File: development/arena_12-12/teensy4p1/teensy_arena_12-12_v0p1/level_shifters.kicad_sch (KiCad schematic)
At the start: 15 parts, among them U1 TXB0108PW, U2 TXB0108PW, U3 TXB0108PW, U4 TXB0108PW, U5 TXB0108PW

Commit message: Worked on 12-12 teensy4p1 arena without vreg.
Modified SPI connections from teensy to panel columns so that all
signals go from a single source to a single destinatin. Also, added
source termination resistors and schmitt trigger buffers to all SPI
signals.
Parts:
- removed U4, U5: TXB0108PW, Package_SO:TSSOP-20_4.4x6.5mm_P0.65mm, symbol TXB0108:TXB0108PW
- added C13, C14, C15, C16, C17, C18, C19, C20, C21, C22, C23, C24, C25, C26, C27, C28, C29, C30, C31, C32, C33, C34, C35, C36, C37, C38, C39, C40, C41, C42, C43, C44, C45, C46, C47, C48, C49, C50, C51, C52, C53, C54, C55, C56, C57, C58, C59, C60, C61, C62, C63, C64: 0.1uF, Capacitor_SMD:C_0603_1608Metric, symbol Device:C
- added R100, R101, R102, R103, R104, R105, R106, R107, R108, R109, R110, R111, R112, R113, R114, R115, R116, R117, R118, R119, R120, R121, R122, R123, R124, R125, R126, R39, R40, R41, R42, R43, R44, R45, R46, R47, R48, R49, R50, R51, R52, R53, R54, R55, R56, R57, R58, R59, R60, R61, R62, R63, R64, R65, R66, R67, R68, R69, R70, R71, R72, R73, R74, R75, R76, R77, R78, R79, R80, R81, R82, R83, R84, R85, R86, R87, R88, R89, R90, R91, R92, R93, R94, R95, R96, R97, R98, R99: 68, symbol Device:R
- added U10, U11, U12, U13, U14, U15, U7, U8, U9: TXB0108PW, Package_SO:TSSOP-20_4.4x6.5mm_P0.65mm, symbol TXB0108:TXB0108PW
- added U16, U17, U18, U19, U20, U21, U22, U23, U24, U25, U26, U27, U28, U29, U30, U31, U32, U33, U34, U35, U36, U37, U38, U39, U40, U41, U42, U43, U44, U45, U46, U47, U48, U49, U50, U51, U52, U53: 74LVC1G17, symbol 74xGxx:74LVC1G17
- renumbered C8 to C10, C9 to C11, C10 to C12, C1 to C3, C2 to C4, C3 to C5, C4 to C6, C5 to C7, C6 to C8, C7 to C9, U1 to U4, U2 to U5, U3 to U6
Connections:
- net +3.3V: now also C13.1, C15.1, C17.1, C19.1, C21.1, C23.1, C25.1, C27.1, C28.1, C29.1, C30.1, C31.1, C32.1, C33.1, C34.1, C35.1, C36.1, C37.1, C38.1, C39.1, C40.1, C41.1, C42.1, C43.1, C44.1, C45.1, C46.1, C47.1, C48.1, C49.1, C50.1, C51.1, C52.1, C53.1, C54.1, C55.1, C56.1, C57.1, C58.1, C59.1, C60.1, C61.1, C62.1, U10.10 (OE), U10.2 (VCCA), U11.10 (OE), U11.2 (VCCA), U12.10 (OE), U12.2 (VCCA), U13.10 (OE), U13.2 (VCCA), U14.10 (OE), U14.2 (VCCA), U15.10 (OE), U15.2 (VCCA), U16.5 (VCC), U17.5 (VCC), U18.5 (VCC), U19.5 (VCC), U20.5 (VCC), U21.5 (VCC), U22.5 (VCC), U23.5 (VCC), U24.5 (VCC), U25.5 (VCC), U26.5 (VCC), U27.5 (VCC), U28.5 (VCC), U29.5 (VCC), U30.5 (VCC), U31.5 (VCC), U32.5 (VCC), U33.5 (VCC), U34.5 (VCC), U35.5 (VCC), U36.5 (VCC), U37.5 (VCC), U38.5 (VCC), U39.5 (VCC), U40.5 (VCC), U41.5 (VCC), U42.5 (VCC), U43.5 (VCC), U44.5 (VCC), U45.5 (VCC), U46.5 (VCC), U47.5 (VCC), U48.5 (VCC), U49.5 (VCC), U50.5 (VCC), U51.5 (VCC), U7.10 (OE), U7.2 (VCCA), U8.10 (OE), U8.2 (VCCA), U9.10 (OE), U9.2 (VCCA)
- net +5V: now also C14.1, C16.1, C18.1, C20.1, C22.1, C24.1, C26.1, C63.1, C64.1, U10.19 (VCCB), U11.19 (VCCB), U12.19 (VCCB), U13.19 (VCCB), U14.19 (VCCB), U15.19 (VCCB), U52.5 (VCC), U53.5 (VCC), U7.19 (VCCB), U8.19 (VCCB), U9.19 (VCCB)
- net GND: now also C13.2, C14.2, C15.2, C16.2, C17.2, C18.2, C19.2, C20.2, C21.2, C22.2, C23.2, C24.2, C25.2, C26.2, C27.2, C28.2, C29.2, C30.2, C31.2, C32.2, C33.2, C34.2, C35.2, C36.2, C37.2, C38.2, C39.2, C40.2, C41.2, C42.2, C43.2, C44.2, C45.2, C46.2, C47.2, C48.2, C49.2, C50.2, C51.2, C52.2, C53.2, C54.2, C55.2, C56.2, C57.2, C58.2, C59.2, C60.2, C61.2, C62.2, C63.2, C64.2, U10.11 (GND), U11.11 (GND), U12.11 (GND), U13.11 (GND), U14.11 (GND), U15.11 (GND), U16.3 (GND), U17.3 (GND), U18.3 (GND), U19.3 (GND), U20.3 (GND), U21.3 (GND), U22.3 (GND), U23.3 (GND), U24.3 (GND), U25.3 (GND), U26.3 (GND), U27.3 (GND), U28.3 (GND), U29.3 (GND), U30.3 (GND), U31.3 (GND), U32.3 (GND), U33.3 (GND), U34.3 (GND), U35.3 (GND), U36.3 (GND), U37.3 (GND), U38.3 (GND), U39.3 (GND), U40.3 (GND), U41.3 (GND), U42.3 (GND), U43.3 (GND), U44.3 (GND), U45.3 (GND), U46.3 (GND), U47.3 (GND), U48.3 (GND), U49.3 (GND), U50.3 (GND), U51.3 (GND), U52.3 (GND), U53.3 (GND), U7.11 (GND), U8.11 (GND), U9.11 (GND)
- net PAN3V.CS_00: now also U20.2; no longer U5.1 (A1)
- net PAN3V.CS_01: now also U21.2; no longer U5.3 (A2)
- net PAN3V.CS_02: now also U22.2; no longer U5.4 (A3)
- net PAN3V.CS_03: now also U23.2; no longer U5.5 (A4)
- net PAN3V.CS_04: now also U24.2; no longer U5.6 (A5)
- net PAN3V.CS_05: now also U25.2; no longer U5.7 (A6)
- net PAN3V.CS_06: now also U26.2; no longer U5.8 (A7)
- net PAN3V.CS_07: now also U27.2; no longer U5.9 (A8)
- net PAN3V.CS_08: now also U28.2; no longer U6.1 (A1)
- net PAN3V.CS_09: now also U29.2; no longer U6.3 (A2)
- net PAN3V.CS_10: now also U30.2; no longer U6.4 (A3)
- net PAN3V.CS_11: now also U31.2; no longer U6.5 (A4)
- net PAN3V.CS_12: now also U32.2; no longer U6.6 (A5)
- net PAN3V.CS_13: now also U33.2; no longer U6.7 (A6)
- net PAN3V.CS_14: now also U34.2; no longer U6.8 (A7)
- net PAN3V.CS_15: now also U35.2; no longer U6.9 (A8)
- net PAN3V.CS_16: now also U36.2
- net PAN3V.CS_17: now also U37.2
- net PAN3V.CS_18: now also U38.2
- net PAN3V.CS_19: now also U39.2
- net PAN3V.CS_20: now also U40.2
- net PAN3V.CS_21: now also U41.2
- net PAN3V.CS_22: now also U42.2
- net PAN3V.CS_23: now also U43.2
- net PAN3V.CS_24: now also U44.2
- net PAN3V.CS_25: now also U45.2
- net PAN3V.CS_26: now also U46.2
- net PAN3V.CS_27: now also U47.2
- net PAN3V.CS_28: now also U48.2
- net PAN3V.CS_29: now also U49.2
- net PAN3V.EXT_INT: now also U51.2
- net PAN3V.MISO_0: now also R125.1; no longer U4.5 (A4)
- net PAN3V.MISO_1: now also R126.1; no longer U4.9 (A8)
- net PAN3V.MOSI_0: now also U17.2; no longer U4.4 (A3)
- net PAN3V.MOSI_1: now also U19.2; no longer U4.8 (A7)
- net PAN3V.RESET: now also U50.2; no longer U4.1 (A1)
- net PAN3V.SCK_0: now also U16.2; no longer U4.3 (A2)
- net PAN3V.SCK_1: now also U18.2; no longer U4.7 (A6)
- net PAN5V.EXT_INT: now also R124.1
- net PAN5V.MISO_0: now also U52.2; no longer U4.16 (B4)
- net PAN5V.MISO_1: now also U53.2; no longer U4.12 (B8)
- net PAN5V.RESET: now also R123.1; no longer U4.20 (B1)
- net PAN5V.CS_00: no longer names the net of U5.20 (B1)
- net PAN5V.CS_00: now also R45.2
- net PAN5V.CS_01: no longer names the net of U5.18 (B2)
- net PAN5V.CS_01: now also R46.2
- net PAN5V.CS_02: no longer names the net of U5.17 (B3)
- net PAN5V.CS_03: no longer names the net of U5.16 (B4)
- net PAN5V.CS_03: now also R47.2
- net PAN5V.CS_04: no longer names the net of U5.15 (B5)
- net PAN5V.CS_05: no longer names the net of U5.14 (B6)
- net PAN5V.CS_05: now also R48.2
- net PAN5V.CS_06: no longer names the net of U5.13 (B7)
- net PAN5V.CS_06: now also R49.2
- net PAN5V.CS_07: no longer names the net of U5.12 (B8)
- net PAN5V.CS_07: now also R50.2
- net PAN5V.CS_08: no longer names the net of U6.20 (B1)
- net PAN5V.CS_08: now also R51.2
- net PAN5V.CS_09: no longer names the net of U6.18 (B2)
- net PAN5V.CS_09: now also R52.2
- net PAN5V.CS_10: no longer names the net of U6.17 (B3)
- net PAN5V.CS_11: no longer names the net of U6.16 (B4)
- net PAN5V.CS_11: now also R53.2
- net PAN5V.CS_12: no longer names the net of U6.15 (B5)
- net PAN5V.CS_13: no longer names the net of U6.14 (B6)
- net PAN5V.CS_13: now also R54.2
- net PAN5V.CS_14: no longer names the net of U6.13 (B7)
- net PAN5V.CS_14: now also R55.2
- net PAN5V.CS_15: no longer names the net of U6.12 (B8)
- net PAN5V.CS_15: now also R56.2
- net PAN5V.MOSI_0: no longer names the net of U4.17 (B3)
- net PAN5V.MOSI_1: no longer names the net of U4.13 (B7)
- net PAN5V.MOSI_1: now also R43.2
- net PAN5V.SCK_0: no longer names the net of U4.18 (B2)
- net PAN5V.SCK_0: now also R40.2
- net PAN5V.SCK_1: no longer names the net of U4.14 (B6)
- net PAN5V.SCK_1: now also R42.2
- new net: U11.1 (A1), U11.3 (A2), U32.4
- new net: R94.2, U11.12 (B8)
- new net: R93.2, U11.13 (B7)
- new net: R92.2, U11.14 (B6)
- new net: R91.2, U11.15 (B5)
- new net: R90.2, U11.16 (B4)
- new net: R89.2, U11.17 (B3)
- new net: R88.2, U11.18 (B2)
- new net: R87.2, U11.20 (B1)
- new net: U11.4 (A3), U11.5 (A4), U33.4
- new net: U11.6 (A5), U11.7 (A6), U34.4
- new net: U11.8 (A7), U11.9 (A8), U35.4
- new net: R57.2, U7.20 (B1)
- new net: R122.2, U15.16 (B4)
- new net: R102.2, U12.12 (B8)
- new net: R86.2, U10.12 (B8)
- new net: R108.2, U13.14 (B6)
- new net: U21.4, U8.4 (A3), U8.5 (A4)
- new net: U13.1 (A1), U13.3 (A2), U40.4
- new net: R107.2, U13.15 (B5)
- new net: U15.1 (A1), U15.3 (A2), U48.4
- new net: R64.2, U8.17 (B3)
- new net: R79.2, U10.20 (B1)
- new net: U14.6 (A5), U14.7 (A6), U46.4
- new net: R73.2, U9.17 (B3)
- new net: U15.12 (B8), U53.4
- new net: U15.13 (B7), U52.4
- new net: R124.2, U15.14 (B6)
- new net: R123.2, U15.15 (B5)
- new net: R121.2, U15.17 (B3)
- new net: R120.2, U15.18 (B2)
- new net: R119.2, U15.20 (B1)
- new net: U15.4 (A3), U15.5 (A4), U49.4
- new net: U15.6 (A5), U50.4
- new net: U15.7 (A6), U51.4
- new net: R125.2, U15.8 (A7)
- new net: R126.2, U15.9 (A8)
- new net: R83.2, U10.15 (B5)
- new net: R77.2, U9.13 (B7)
- new net: R116.2, U14.14 (B6)
- new net: U27.4, U9.8 (A7), U9.9 (A8)
- new net: R68.2, U8.13 (B7)
- new net: R78.2, U9.12 (B8)
- new net: U13.6 (A5), U13.7 (A6), U42.4
- new net: R59.2, U7.16 (B4)
- new net: U14.1 (A1), U14.3 (A2), U44.4
- new net: R118.2, U14.12 (B8)
- new net: R117.2, U14.13 (B7)
- new net: R115.2, U14.15 (B5)
- new net: R114.2, U14.16 (B4)
- new net: R113.2, U14.17 (B3)
- new net: R112.2, U14.18 (B2)
- new net: R111.2, U14.20 (B1)
- new net: U14.4 (A3), U14.5 (A4), U45.4
- new net: U14.8 (A7), U14.9 (A8), U47.4
- new net: R97.2, U12.17 (B3)
- new net: U26.4, U9.6 (A5), U9.7 (A6)
- new net: U16.4, U4.1 (A1), U4.3 (A2), U4.5 (A4), U4.7 (A6), U4.8 (A7), U4.9 (A8)
- new net: R44.2, U4.12 (B8)
- new net: R41.2, U4.16 (B4)
- new net: R39.2, U4.20 (B1)
- new net: R84.2, U10.14 (B6)
- new net: R104.2, U13.18 (B2)
- new net: R62.2, U7.12 (B8)
- new net: U12.6 (A5), U12.7 (A6), U38.4
- new net: U13.4 (A3), U13.5 (A4), U41.4
- new net: U10.1 (A1), U10.3 (A2), U28.4
- new net: R85.2, U10.13 (B7)
- new net: R82.2, U10.16 (B4)
- new net: R81.2, U10.17 (B3)
- new net: R80.2, U10.18 (B2)
- new net: U10.4 (A3), U10.5 (A4), U29.4
- new net: U10.6 (A5), U10.7 (A6), U30.4
- new net: U10.8 (A7), U10.9 (A8), U31.4
- new net: R67.2, U8.14 (B6)
- new net: R109.2, U13.13 (B7)
- new net: R76.2, U9.14 (B6)
- new net: R96.2, U12.18 (B2)
- new net: R66.2, U8.15 (B5)
- new net: R74.2, U9.16 (B4)
- new net: R58.2, U7.18 (B2)
- new net: R95.2, U12.20 (B1)
- new net: R69.2, U8.20 (B1)
- new net: R98.2, U12.16 (B4)
- new net: R65.2, U8.16 (B4)
- new net: U20.4, U8.1 (A1), U8.3 (A2)
- new net: U12.8 (A7), U12.9 (A8), U39.4
- new net: U13.8 (A7), U13.9 (A8), U43.4
- new net: U19.4, U7.1 (A1), U7.3 (A2), U7.5 (A4), U7.7 (A6), U7.8 (A7), U7.9 (A8)
- new net: R110.2, U13.12 (B8)
- new net: R106.2, U13.16 (B4)
- new net: R105.2, U13.17 (B3)
- new net: R103.2, U13.20 (B1)
- new net: U18.4, U6.1 (A1), U6.3 (A2), U6.5 (A4), U6.7 (A6), U6.8 (A7), U6.9 (A8)
- new net: U12.4 (A3), U12.5 (A4), U37.4
- new net: U12.1 (A1), U12.3 (A2), U36.4
- new net: R101.2, U12.13 (B7)
- new net: R100.2, U12.14 (B6)
- new net: R99.2, U12.15 (B5)
- new net: R72.2, U9.18 (B2)
- new net: U17.4, U5.1 (A1), U5.3 (A2), U5.5 (A4), U5.7 (A6), U5.8 (A7), U5.9 (A8)
- new net: R60.2, U7.14 (B6)
- new net: U23.4, U8.8 (A7), U8.9 (A8)
- new net: U24.4, U9.1 (A1), U9.3 (A2)
- new net: R61.2, U7.13 (B7)
- new net: R70.2, U8.12 (B8)
- new net: R63.2, U8.18 (B2)
- new net: R75.2, U9.15 (B5)
- new net: U25.4, U9.4 (A3), U9.5 (A4)
- new net: U22.4, U8.6 (A5), U8.7 (A6)
- new net: R71.2, U9.20 (B1)
- new net PAN5V.CS_00_P1: R69.1
- new net PAN5V.CS_00_P7: R63.1
- new net PAN5V.CS_01_P1: R64.1
- new net PAN5V.CS_01_P7: R65.1
- new net PAN5V.CS_02_P1: R66.1
- new net PAN5V.CS_02_P7: R67.1
- new net PAN5V.CS_03_P1: R68.1
- new net PAN5V.CS_03_P7: R70.1
- new net PAN5V.CS_04_P1: R71.1
- new net PAN5V.CS_04_P7: R72.1
- new net PAN5V.CS_05_P2: R73.1
- new net PAN5V.CS_05_P8: R74.1
- new net PAN5V.CS_06_P2: R75.1
- new net PAN5V.CS_06_P8: R76.1
- new net PAN5V.CS_07_P2: R77.1
- new net PAN5V.CS_07_P8: R78.1
- new net PAN5V.CS_08_P2: R79.1
- new net PAN5V.CS_08_P8: R80.1
- new net PAN5V.CS_09_P2: R81.1
- new net PAN5V.CS_09_P8: R82.1
- new net PAN5V.CS_10_P3: R83.1
- new net PAN5V.CS_10_P9: R84.1
- new net PAN5V.CS_11_P3: R85.1
- new net PAN5V.CS_11_P9: R86.1
- new net PAN5V.CS_12_P3: R87.1
- new net PAN5V.CS_12_P9: R88.1
- new net PAN5V.CS_13_P3: R89.1
- new net PAN5V.CS_13_P9: R90.1
- new net PAN5V.CS_14_P3: R91.1
- new net PAN5V.CS_14_P9: R92.1
- new net PAN5V.CS_15_P10: R94.1
- new net PAN5V.CS_15_P4: R93.1
- new net PAN5V.CS_16_P10: R96.1
- new net PAN5V.CS_16_P4: R95.1
- new net PAN5V.CS_17_P10: R98.1
- new net PAN5V.CS_17_P4: R97.1
- new net PAN5V.CS_18_P10: R100.1
- new net PAN5V.CS_18_P4: R99.1
- new net PAN5V.CS_19_P10: R102.1
- new net PAN5V.CS_19_P4: R101.1
- new net PAN5V.CS_20_P11: R104.1
- new net PAN5V.CS_20_P5: R103.1
- new net PAN5V.CS_21_P11: R106.1
- new net PAN5V.CS_21_P5: R105.1
- new net PAN5V.CS_22_P11: R108.1
- new net PAN5V.CS_22_P5: R107.1
- new net PAN5V.CS_23_P11: R110.1
- new net PAN5V.CS_23_P5: R109.1
- new net PAN5V.CS_24_P11: R112.1
- new net PAN5V.CS_24_P5: R111.1
- new net PAN5V.CS_25_P12: R114.1
- new net PAN5V.CS_25_P6: R113.1
- new net PAN5V.CS_26_P12: R116.1
- new net PAN5V.CS_26_P6: R115.1
- new net PAN5V.CS_27_P12: R118.1
- new net PAN5V.CS_27_P6: R117.1
- new net PAN5V.CS_28_P12: R120.1
- new net PAN5V.CS_28_P6: R119.1
- new net PAN5V.CS_29_P12: R122.1
- new net PAN5V.CS_29_P6: R121.1
- new net PAN5V.MOSI_0_P1: R45.1
- new net PAN5V.MOSI_0_P2: R46.1
- new net PAN5V.MOSI_0_P3: R47.1
- new net PAN5V.MOSI_0_P4: R48.1
- new net PAN5V.MOSI_0_P5: R49.1
- new net PAN5V.MOSI_0_P6: R50.1
- new net PAN5V.MOSI_1_P10: R60.1
- new net PAN5V.MOSI_1_P11: R61.1
- new net PAN5V.MOSI_1_P12: R62.1
- new net PAN5V.MOSI_1_P7: R57.1
- new net PAN5V.MOSI_1_P8: R58.1
- new net PAN5V.MOSI_1_P9: R59.1
- new net PAN5V.SCK_0_P1: R39.1
- new net PAN5V.SCK_0_P2: R40.1
- new net PAN5V.SCK_0_P3: R41.1
- new net PAN5V.SCK_0_P4: R42.1
- new net PAN5V.SCK_0_P5: R43.1
- new net PAN5V.SCK_0_P6: R44.1
- new net PAN5V.SCK_1_P10: R54.1
- new net PAN5V.SCK_1_P11: R55.1
- new net PAN5V.SCK_1_P12: R56.1
- new net PAN5V.SCK_1_P7: R51.1
- new net PAN5V.SCK_1_P8: R52.1
- new net PAN5V.SCK_1_P9: R53.1
- no-connect marks 4 -> 54
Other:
- moved on the sheet: C10, C11, C12, C3, C4, C5, C6, C7, C8, C9, U4, U5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

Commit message: More work on schematic for 12-12 teensy arena.
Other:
- moved on the sheet: C10, C11, C12, C13, C14, C15, C16, C17, C18, C20, C21, C22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

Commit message: Reworked schematic for 12-12 teensy arena w/o regulators some more.
Worked on foot print assignmets. Started replacing some of the single
schmitt triggers with equivalent dual versions to reduce component
count.
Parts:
- removed C32, C33, C34: 0.1uF, Capacitor_SMD:C_0603_1608Metric, symbol Device:C
- removed U20, U21, U22, U23: 74LVC1G17, symbol 74xGxx:74LVC1G17
- added C31: 0.1uF, Capacitor_SMD:C_0603_1608Metric, symbol Device:C
- added U19, U20: 74LVC2G17, symbol 74xGxx:74LVC2G17
- R100, R101, R102, R103, R104, R105, R106, R107, R108, R109, R110, R111, R112, R113, R114, R115, R116, R117, R118, R119, R120, R121, R122, R123, R124, R125, R126, R39, R40, R41, R42, R43, R44, R45, R46, R47, R48, R49, R50, R51, R52, R53, R54, R55, R56, R57, R58, R59, R60, R61, R62, R63, R64, R65, R66, R67, R68, R69, R70, R71, R72, R73, R74, R75, R76, R77, R78, R79, R80, R81, R82, R83, R84, R85, R86, R87, R88, R89, R90, R91, R92, R93, R94, R95, R96, R97, R98, R99: footprint (none) -> Resistor_SMD:R_0603_1608Metric
- U15: renamed from U16; footprint (none) -> Package_SO:TSSOP-20_4.4x6.5mm_P0.65mm
- U3: renamed from U4; footprint Package_SO:TSSOP-20_4.4x6.5mm_P0.65mm -> (none)
- renumbered C11 to C10, C12 to C11, C13 to C12, C14 to C13, C15 to C14, C16 to C15, C17 to C16, C18 to C17, C19 to C18, C20 to C19, C3 to C2, C21 to C20, C22 to C21, C23 to C22, C24 to C23, C25 to C24, C26 to C25, C27 to C26, C28 to C27, C29 to C28, C30 to C29, C4 to C3, C31 to C30, C5 to C4, C6 to C5, C7 to C6, C8 to C7, C9 to C8, C10 to C9, U11 to U10, U12 to U11, U13 to U12, U14 to U13, U15 to U14, U17 to U16, U18 to U17, U19 to U18, U5 to U4, U6 to U5, U7 to U6, U8 to U7, U9 to U8, U10 to U9
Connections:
- net +3.3V: now also C31.1, U19.5 (VCC), U20.5 (VCC)
- net GND: now also C31.2, U19.2 (GND), U20.2 (GND)
- net PAN3V.CS_00: now also U19.1
- net PAN3V.CS_01: now also U19.3
- net PAN3V.CS_02: now also U20.1
- net PAN3V.CS_03: now also U20.3
- net at U7.4 (A3), U7.5 (A4): now also U19.4
- net at U7.1 (A1), U7.3 (A2): now also U19.6
- net at U7.8 (A7), U7.9 (A8): now also U20.4
- net at U7.6 (A5), U7.7 (A6): now also U20.6
- no-connect marks 54 -> 50
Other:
- moved on the sheet: C10, C11, C12, C13, C14, C15, C16, C17, C18, C19, C20, C21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

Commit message: Finished initial schematic for 12-12 teensy 4.1 arena w/o vreg.
Finished footprint assignments and started working on layout changes.
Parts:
- removed C47, C48, C49, C50, C51, C52, C53, C54, C55, C56, C57, C58, C59, C60, C61, C62, C63, C64: 0.1uF, Capacitor_SMD:C_0603_1608Metric, symbol Device:C
- removed U24, U25, U26, U27, U28, U29, U30, U31, U32, U33, U34, U35, U36, U37, U38, U39, U40, U41, U42, U43, U44, U45, U46, U47, U48, U49, U50, U51, U52, U53: 74LVC1G17, symbol 74xGxx:74LVC1G17
- added C32, C33, C34: 0.1uF, Capacitor_SMD:C_0603_1608Metric, symbol Device:C
- added U21, U22, U23, U24, U25, U26, U27, U28, U29, U30, U31, U32, U33, U34, U35: 74LVC2G17, Package_TO_SOT_SMD:SOT-23-6, symbol 74xGxx:74LVC2G17
- U15: footprint Package_SO:TSSOP-20_4.4x6.5mm_P0.65mm -> Package_TO_SOT_SMD:SOT-23-5
- U16, U17, U18: footprint (none) -> Package_TO_SOT_SMD:SOT-23-5
- U19, U20: footprint (none) -> Package_TO_SOT_SMD:SOT-23-6
- U3: footprint (none) -> Package_SO:TSSOP-20_4.4x6.5mm_P0.65mm
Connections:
- net +3.3V: now also C32.1, C33.1, C34.1, U21.5 (VCC), U22.5 (VCC), U23.5 (VCC), U24.5 (VCC), U25.5 (VCC), U26.5 (VCC), U27.5 (VCC), U28.5 (VCC), U29.5 (VCC), U30.5 (VCC), U31.5 (VCC), U32.5 (VCC), U33.5 (VCC), U34.5 (VCC), U35.5 (VCC)
- net GND: now also C32.2, C33.2, C34.2, U21.2 (GND), U22.2 (GND), U23.2 (GND), U24.2 (GND), U25.2 (GND), U26.2 (GND), U27.2 (GND), U28.2 (GND), U29.2 (GND), U30.2 (GND), U31.2 (GND), U32.2 (GND), U33.2 (GND), U34.2 (GND), U35.2 (GND)
- net PAN3V.CS_04: now also U21.1
- net PAN3V.CS_05: now also U21.3
- net PAN3V.CS_06: now also U22.1
- net PAN3V.CS_07: now also U22.3
- net PAN3V.CS_08: now also U23.1
- net PAN3V.CS_09: now also U23.3
- net PAN3V.CS_10: now also U24.1
- net PAN3V.CS_11: now also U24.3
- net PAN3V.CS_12: now also U25.1
- net PAN3V.CS_13: now also U25.3
- net PAN3V.CS_14: now also U26.1
- net PAN3V.CS_15: now also U26.3
- net PAN3V.CS_16: now also U27.1
- net PAN3V.CS_17: now also U27.3
- net PAN3V.CS_18: now also U28.1
- net PAN3V.CS_19: now also U28.3
- net PAN3V.CS_20: now also U29.1
- net PAN3V.CS_21: now also U29.3
- net PAN3V.CS_22: now also U30.1
- net PAN3V.CS_23: now also U30.3
- net PAN3V.CS_24: now also U31.1
- net PAN3V.CS_25: now also U31.3
- net PAN3V.CS_26: now also U32.1
- net PAN3V.CS_27: now also U32.3
- net PAN3V.CS_28: now also U33.1
- net PAN3V.CS_29: now also U33.3
- net PAN3V.EXT_INT: now also U34.3
- net PAN3V.RESET: now also U34.1
- net PAN5V.MISO_0: now also U35.1
- net PAN5V.MISO_1: now also U35.3
- net at U10.1 (A1), U10.3 (A2): now also U25.6
- net at U10.4 (A3), U10.5 (A4): now also U25.4
- net at U10.6 (A5), U10.7 (A6): now also U26.6
- net at U10.8 (A7), U10.9 (A8): now also U26.4
- net at U12.1 (A1), U12.3 (A2): now also U29.6
- net at U14.1 (A1), U14.3 (A2): now also U33.6
- net at U13.6 (A5), U13.7 (A6): now also U32.6
- net at U14.12 (B8): now also U35.4
- net at U14.13 (B7): now also U35.6
- net at U14.4 (A3), U14.5 (A4): now also U33.4
- net at U14.6 (A5): now also U34.6
- net at U14.7 (A6): now also U34.4
- net at U8.8 (A7), U8.9 (A8): now also U22.4
- net at U12.6 (A5), U12.7 (A6): now also U30.6
- net at U13.1 (A1), U13.3 (A2): now also U31.6
- net at U13.4 (A3), U13.5 (A4): now also U31.4
- net at U13.8 (A7), U13.9 (A8): now also U32.4
- net at U8.6 (A5), U8.7 (A6): now also U22.6
- net at U11.6 (A5), U11.7 (A6): now also U28.6
- net at U12.4 (A3), U12.5 (A4): now also U29.4
- net at U9.1 (A1), U9.3 (A2): now also U23.6
- net at U9.4 (A3), U9.5 (A4): now also U23.4
- net at U9.6 (A5), U9.7 (A6): now also U24.6
- net at U9.8 (A7), U9.9 (A8): now also U24.4
- net at U11.8 (A7), U11.9 (A8): now also U28.4
- net at U12.8 (A7), U12.9 (A8): now also U30.4
- net at U11.4 (A3), U11.5 (A4): now also U27.4
- net at U11.1 (A1), U11.3 (A2): now also U27.6
- net at U8.1 (A1), U8.3 (A2): now also U21.6
- net at U8.4 (A3), U8.5 (A4): now also U21.4
- no-connect marks 50 -> 20
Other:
- note added: "SN74LVC1G17DBVR C7836"
- moved on the sheet: R125, R126

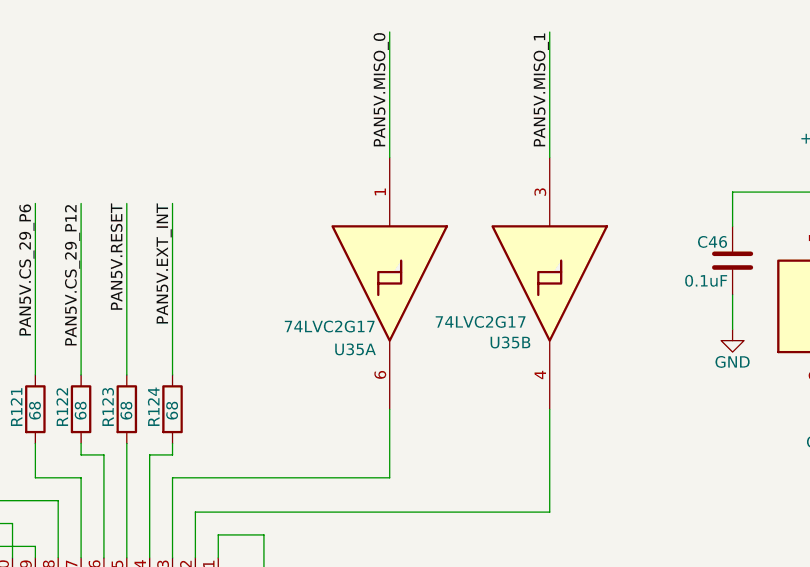
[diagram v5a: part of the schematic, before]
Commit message: Finished preliminary layout for new 12-12 teensy 4.1 arena.
Includes source termination resistors and schmitt trigger buffers.
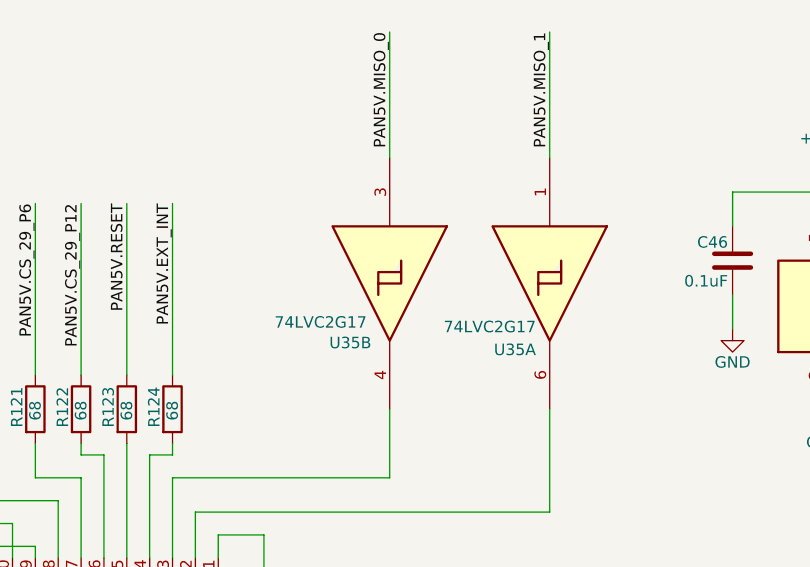
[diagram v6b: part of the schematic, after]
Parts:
- C10, C11, C12, C13, C14, C15, C16, C17, C18, C19, C2, C20, C21, C22, C23, C24, C25, C26, C27, C28, C29, C3, C30, C31, C32, C33, C34, C35, C36, C37, C38, C39, C4, C40, C41, C42, C43, C44, C45, C46, C5, C6, C7, C8, C9: footprint Capacitor_SMD:C_0603_1608Metric -> Capacitor_SMD:C_0402_1005Metric
- R100, R101, R102, R103, R104, R105, R106, R107, R108, R109, R110, R111, R112, R113, R114, R115, R116, R117, R118, R119, R120, R121, R122, R123, R124, R125, R126, R39, R40, R41, R42, R43, R44, R45, R46, R47, R48, R49, R50, R51, R52, R53, R54, R55, R56, R57, R58, R59, R60, R61, R62, R63, R64, R65, R66, R67, R68, R69, R70, R71, R72, R73, R74, R75, R76, R77, R78, R79, R80, R81, R82, R83, R84, R85, R86, R87, R88, R89, R90, R91, R92, R93, R94, R95, R96, R97, R98, R99: footprint Resistor_SMD:R_0603_1608Metric -> Resistor_SMD:R_0402_1005Metric
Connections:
- net PAN5V.MISO_0: now also U35.3; no longer U35.1
- net PAN5V.MISO_1: now also U35.1; no longer U35.3
- net at U14.12 (B8): now also U35.6; no longer U35.4
- net at U14.13 (B7): now also U35.4; no longer U35.6
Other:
- moved on the sheet: U35A, U35B

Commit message: Worked on prelimnary hand routing of 12-12 teensy 4.1 arena.
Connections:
- net PAN3V.CS_04: now also U22.1; no longer U21.1
- net PAN3V.CS_05: now also U22.3; no longer U21.3
- net PAN3V.CS_06: now also U21.1; no longer U22.1
- net PAN3V.CS_07: now also U21.3; no longer U22.3
- net PAN3V.CS_12: now also U26.1; no longer U25.1
- net PAN3V.CS_13: now also U26.3; no longer U25.3
- net PAN3V.CS_14: now also U25.1; no longer U26.1
- net PAN3V.CS_15: now also U25.3; no longer U26.3
- net at U10.1 (A1), U10.3 (A2): now also U26.6; no longer U25.6
- net at U10.4 (A3), U10.5 (A4): now also U26.4; no longer U25.4
- net at U10.6 (A5), U10.7 (A6): now also U25.6; no longer U26.6
- net at U10.8 (A7), U10.9 (A8): now also U25.4; no longer U26.4
- net at U8.6 (A5), U8.7 (A6): now also U21.6; no longer U22.6
- net at U8.4 (A3), U8.5 (A4): now also U22.4; no longer U21.4
- net at U8.1 (A1), U8.3 (A2): now also U22.6; no longer U21.6
- net at U8.8 (A7), U8.9 (A8): now also U21.4; no longer U22.4
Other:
- moved on the sheet: U21A, U21B, U22A, U22B, U25A, U25B, U26A, U26B
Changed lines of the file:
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@@
 	(symbol
 		(lib_id "74xGxx:74LVC2G17")
-		(at 584.2 273.05 90)
+		(at 621.03 273.05 90)
 		(unit 1)
 		(exclude_from_sim no)
@@
 		(dnp no)
 		(property "Reference" "U25"
-			(at 586.486 267.97 90)
+			(at 623.316 267.97 90)
 			(effects
 				(font
@@
 		)
 		(property "Value" "74LVC2G17"
-			(at 586.486 270.51 90)
+			(at 623.316 270.51 90)
 			(effects
 				(font
@@
 		)
 		(property "Footprint" "Package_TO_SOT_SMD:SOT-23-6"
-			(at 584.2 273.05 0)
+			(at 621.03 273.05 0)
 			(effects
 				(font
@@
 		)
 		(property "Datasheet" "http://www.ti.com/lit/sg/scyt129e/scyt129e.pdf"
-			(at 584.2 273.05 0)
+			(at 621.03 273.05 0)
 			(effects
 				(font
@@
 		)
 		(property "Description" "Dual Buffer Schmitt Triggered, Low-Voltage CMOS"
-			(at 584.2 273.05 0)
+			(at 621.03 273.05 0)
 			(effects
 				(font
@@
 	(symbol
 		(lib_id "74xGxx:74LVC2G17")
-		(at 295.91 275.59 90)
+		(at 259.08 275.59 90)
 		(unit 1)
 		(exclude_from_sim no)
@@
 		(dnp no)
 		(property "Reference" "U22"
-			(at 297.434 269.494 90)
+			(at 260.604 269.494 90)
 			(effects
 				(font
@@
 		)
 		(property "Value" "74LVC2G17"
-			(at 297.434 272.034 90)
+			(at 260.604 272.034 90)
 			(effects
 				(font
@@
 		)
 		(property "Footprint" "Package_TO_SOT_SMD:SOT-23-6"
-			(at 295.91 275.59 0)
+			(at 259.08 275.59 0)
 			(effects
 				(font
@@
 		)
 		(property "Datasheet" "http://www.ti.com/lit/sg/scyt129e/scyt129e.pdf"
-			(at 295.91 275.59 0)
+			(at 259.08 275.59 0)
 			(effects
 				(font
@@
 		)
 		(property "Description" "Dual Buffer Schmitt Triggered, Low-Voltage CMOS"
-			(at 295.91 275.59 0)
+			(at 259.08 275.59 0)
 			(effects
 				(font
@@
 	(symbol
 		(lib_id "74xGxx:74LVC2G17")
-		(at 278.13 275.59 90)
+		(at 314.96 275.59 90)
 		(unit 2)
 		(exclude_from_sim no)
@@
 		(dnp no)
 		(property "Reference" "U21"
-			(at 280.924 271.272 90)
+			(at 317.754 271.272 90)
 			(effects
 				(font
@@
 		)
 		(property "Value" "74LVC2G17"
-			(at 280.416 273.304 90)
+			(at 317.246 273.304 90)
 			(effects
 				(font
@@
 		)
 		(property "Footprint" "Package_TO_SOT_SMD:SOT-23-6"
-			(at 278.13 275.59 0)
+			(at 314.96 275.59 0)
 			(effects
 				(font
@@
 		)
 		(property "Datasheet" "http://www.ti.com/lit/sg/scyt129e/scyt129e.pdf"
-			(at 278.13 275.59 0)
+			(at 314.96 275.59 0)
 			(effects
 				(font
@@
 		)
 		(property "Description" "Dual Buffer Schmitt Triggered, Low-Voltage CMOS"
-			(at 278.13 275.59 0)
+			(at 314.96 275.59 0)
 			(effects
 				(font
@@
 	(symbol
 		(lib_id "74xGxx:74LVC2G17")
-		(at 259.08 275.59 90)
+		(at 295.91 275.59 90)
 		(unit 1)
 		(exclude_from_sim no)
@@
 		(dnp no)
 		(property "Reference" "U21"
-			(at 261.366 270.51 90)
+			(at 298.196 270.51 90)
 			(effects
 				(font
@@
 		)
 		(property "Value" "74LVC2G17"
-			(at 261.366 273.05 90)
+			(at 298.196 273.05 90)
 			(effects
 				(font
@@
 		)
 		(property "Footprint" "Package_TO_SOT_SMD:SOT-23-6"
-			(at 259.08 275.59 0)
+			(at 295.91 275.59 0)
 			(effects
 				(font
@@
 		)
 		(property "Datasheet" "http://www.ti.com/lit/sg/scyt129e/scyt129e.pdf"
-			(at 259.08 275.59 0)
+			(at 295.91 275.59 0)
 			(effects
 				(font
@@
 		)
 		(property "Description" "Dual Buffer Schmitt Triggered, Low-Voltage CMOS"
-			(at 259.08 275.59 0)
+			(at 295.91 275.59 0)
 			(effects
 				(font
@@
 	(symbol
 		(lib_id "74xGxx:74LVC2G17")
-		(at 621.03 273.05 90)
+		(at 584.2 273.05 90)
 		(unit 1)
 		(exclude_from_sim no)
@@
 		(dnp no)
 		(property "Reference" "U26"
-			(at 622.554 266.954 90)
+			(at 585.724 266.954 90)
 			(effects
 				(font
@@
 		)
 		(property "Value" "74LVC2G17"
-			(at 622.554 269.494 90)
+			(at 585.724 269.494 90)
 			(effects
 				(font
@@
 		)
 		(property "Footprint" "Package_TO_SOT_SMD:SOT-23-6"
-			(at 621.03 273.05 0)
+			(at 584.2 273.05 0)
 			(effects
 				(font
@@
 		)
 		(property "Datasheet" "http://www.ti.com/lit/sg/scyt129e/scyt129e.pdf"
-			(at 621.03 273.05 0)
+			(at 584.2 273.05 0)
 			(effects
 				(font
@@
 		)
 		(property "Description" "Dual Buffer Schmitt Triggered, Low-Voltage CMOS"
-			(at 621.03 273.05 0)
+			(at 584.2 273.05 0)
 			(effects
 				(font
@@
 	(symbol
 		(lib_id "74xGxx:74LVC2G17")
-		(at 603.25 273.05 90)
+		(at 640.08 273.05 90)
 		(unit 2)
 		(exclude_from_sim no)
@@
 		(dnp no)
 		(property "Reference" "U25"
-			(at 606.044 268.732 90)
+			(at 642.874 268.732 90)
 			(effects
 				(font
@@
 		)
 		(property "Value" "74LVC2G17"
-			(at 605.536 270.764 90)
+			(at 642.366 270.764 90)
 			(effects
 				(font
@@
 		)
 		(property "Footprint" "Package_TO_SOT_SMD:SOT-23-6"
-			(at 603.25 273.05 0)
+			(at 640.08 273.05 0)
 			(effects
 				(font
@@
 		)
 		(property "Datasheet" "http://www.ti.com/lit/sg/scyt129e/scyt129e.pdf"
-			(at 603.25 273.05 0)
+			(at 640.08 273.05 0)
 			(effects
 				(font
@@
 		)
 		(property "Description" "Dual Buffer Schmitt Triggered, Low-Voltage CMOS"
-			(at 603.25 273.05 0)
+			(at 640.08 273.05 0)
 			(effects
 				(font
@@
 	(symbol
 		(lib_id "74xGxx:74LVC2G17")
-		(at 314.96 275.59 90)
+		(at 278.13 275.59 90)
 		(unit 2)
 		(exclude_from_sim no)
@@
 		(dnp no)
 		(property "Reference" "U22"
-			(at 316.992 270.256 90)
+			(at 280.162 270.256 90)
 			(effects
 				(font
@@
 		)
 		(property "Value" "74LVC2G17"
-			(at 317.5 272.542 90)
+			(at 280.67 272.542 90)
 			(effects
 				(font
@@
 		)
 		(property "Footprint" "Package_TO_SOT_SMD:SOT-23-6"
-			(at 314.96 275.59 0)
+			(at 278.13 275.59 0)
 			(effects
 				(font
@@
 		)
 		(property "Datasheet" "http://www.ti.com/lit/sg/scyt129e/scyt129e.pdf"
-			(at 314.96 275.59 0)
+			(at 278.13 275.59 0)
 			(effects
 				(font
@@
 		)
 		(property "Description" "Dual Buffer Schmitt Triggered, Low-Voltage CMOS"
-			(at 314.96 275.59 0)
+			(at 278.13 275.59 0)
 			(effects
 				(font
@@
 	(symbol
 		(lib_id "74xGxx:74LVC2G17")
-		(at 640.08 273.05 90)
+		(at 603.25 273.05 90)
 		(unit 2)
 		(exclude_from_sim no)
@@
 		(dnp no)
 		(property "Reference" "U26"
-			(at 642.112 267.716 90)
+			(at 605.282 267.716 90)
 			(effects
 				(font
@@
 		)
 		(property "Value" "74LVC2G17"
-			(at 642.62 270.002 90)
+			(at 605.79 270.002 90)
 			(effects
 				(font
@@
 		)
 		(property "Footprint" "Package_TO_SOT_SMD:SOT-23-6"
-			(at 640.08 273.05 0)
+			(at 603.25 273.05 0)
 			(effects
 				(font
@@
 		)
 		(property "Datasheet" "http://www.ti.com/lit/sg/scyt129e/scyt129e.pdf"
-			(at 640.08 273.05 0)
+			(at 603.25 273.05 0)
 			(effects
 				(font
@@
 		)
 		(property "Description" "Dual Buffer Schmitt Triggered, Low-Voltage CMOS"
-			(at 640.08 273.05 0)
+			(at 603.25 273.05 0)
 			(effects
 				(font

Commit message: Finished initial verions of fab files for 12-12 teensy 4.1 arena. Need to check orientations.
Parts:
- R100, R101, R102, R103, R104, R105, R106, R107, R108, R109, R110, R111, R112, R113, R114, R115, R116, R117, R118, R119, R120, R121, R122, R123, R124, R125, R126, R39, R40, R41, R42, R43, R44, R45, R46, R47, R48, R49, R50, R51, R52, R53, R54, R55, R56, R57, R58, R59, R60, R61, R62, R63, R64, R65, R66, R67, R68, R69, R70, R71, R72, R73, R74, R75, R76, R77, R78, R79, R80, R81, R82, R83, R84, R85, R86, R87, R88, R89, R90, R91, R92, R93, R94, R95, R96, R97, R98, R99: value 68 -> 33
